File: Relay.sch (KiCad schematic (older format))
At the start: 0 parts

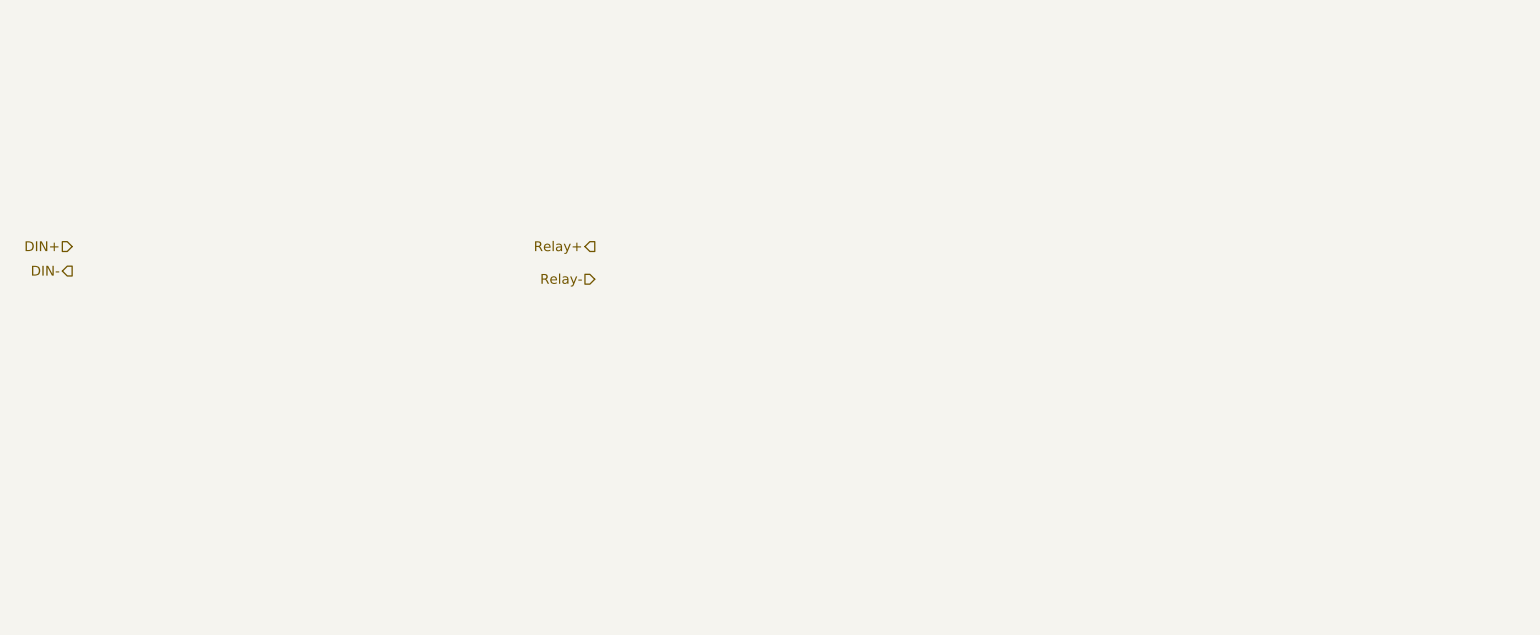
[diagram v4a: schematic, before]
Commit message: Added Relay Driver
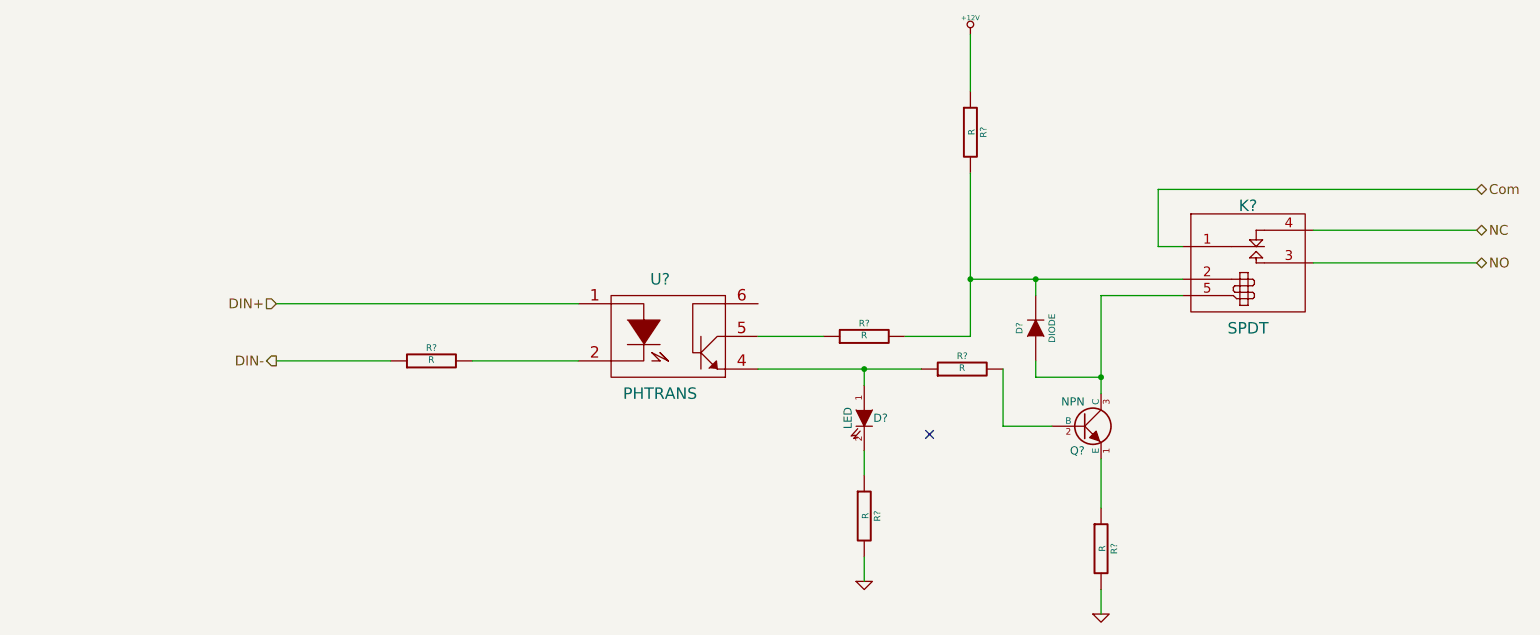
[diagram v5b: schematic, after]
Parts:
- added D?: LED, ~, symbol LED
- added D?: DIODE, ~, symbol DIODE
- added K?: SPDT, ~, symbol SPDT
- added Q?: NPN, ~, symbol NPN
- added R? (x6): R, ~, symbol R
- added U?: PHTRANS, ~, symbol PHTRANS
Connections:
- net DIN+: now also U?.1
- net DIN-: now also R?.1
- new net: R?.2, U?.2
- new net: D?.1 (A), R?.1, U?.4
- new net: R?.1, U?.5
- new net: Q?.1 (E), R?.1
- new net: Q?.2 (B), R?.2
- new net: D?.1 (A), K?.5 (Coil-), Q?.3 (C)
- new net: D?.2 (K), R?.1
- new net: D?.2 (K), K?.2 (Coil-), R?.2, R?.2
- new net +12V: R?.1
- new net Com: K?.1 (Com)
- new net GND: R?.2, R?.2
- new net NC: K?.4 (NC)
- new net NO: K?.3 (NO)
- no-connect marks 0 -> 1
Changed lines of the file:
@@
 LIBS:contrib
 LIBS:valves
+LIBS:arduino_shieldsNCL
+LIBS:spdt
 LIBS:InitialKiCadProject-cache
 EELAYER 27 0
@@
 Comment4 ""
 $EndDescr
-Text HLabel 5350 2800 0    60   Input ~ 0
-Relay-
-Text HLabel 5350 2600 0    60   Output ~ 0
-Relay+
-Text HLabel 2150 2750 0    60   Output ~ 0
+Text HLabel 10750 2700 2    60   BiDi ~ 0
+NO
+Text HLabel 10750 2500 2    60   BiDi ~ 0
+NC
+Text HLabel 3400 3300 0    60   Output ~ 0
 DIN-
-Text HLabel 2150 2600 0    60   Input ~ 0
+Text HLabel 3400 2950 0    60   Input ~ 0
 DIN+
+$Comp
+L PHTRANS U?
+U 1 1 52F444EE
+P 5800 3150
+F 0 "U?" H 5750 3500 70  0000 C CNN
+F 1 "PHTRANS" H 5750 2800 70  0000 C CNN
+F 2 "~" H 5800 3150 60  0000 C CNN
+F 3 "~" H 5800 3150 60  0000 C CNN
+	1    5800 3150
+	1    0    0    -1
+$EndComp
+$Comp
+L NPN Q?
+U 1 1 52F4450C
+P 8350 3700
+F 0 "Q?" H 8350 3550 50  0000 R CNN
+F 1 "NPN" H 8350 3850 50  0000 R CNN
+F 2 "~" H 8350 3700 60  0000 C CNN
+F 3 "~" H 8350 3700 60  0000 C CNN
+	1    8350 3700
+	1    0    0    -1
+$EndComp
+$Comp
+L R R?
+U 1 1 52F4451B
+P 7600 3350
+F 0 "R?" V 7680 3350 40  0000 C CNN
+F 1 "R" V 7607 3351 40  0000 C CNN
+F 2 "~" V 7530 3350 30  0000 C CNN
+F 3 "~" H 7600 3350 30  0000 C CNN
+	1    7600 3350
+	0    -1   -1   0
+$EndComp
+$Comp
+L LED D?
+U 1 1 52F4452A
+P 7000 3650
+F 0 "D?" V 7000 3750 50  0000 C CNN
+F 1 "LED" H 7000 3550 50  0000 C CNN
+F 2 "~" H 7000 3650 60  0000 C CNN
+F 3 "~" H 7000 3650 60  0000 C CNN
+	1    7000 3650
+	0    1    1    0
+$EndComp
+$Comp
+L SPDT K?
+U 1 1 52F44B09
+P 9350 2700
+F 0 "K?" H 9350 3050 70  0000 C CNN
+F 1 "SPDT" H 9350 2300 70  0000 C CNN
+F 2 "~" H 9350 2850 60  0000 C CNN
+F 3 "~" H 9350 2850 60  0000 C CNN
+	1    9350 2700
+	1    0    0    -1
+$EndComp
+Text HLabel 10750 2250 2    60   BiDi ~ 0
+Com
+Wire Wire Line
+	10750 2500 9750 2500
+Wire Wire Line
+	9750 2700 10750 2700
+Wire Wire Line
+	6350 3350 7350 3350
+Wire Wire Line
+	8950 2900 8450 2900
+Wire Wire Line
+	8450 2900 8450 3500
+$Comp
+L R R?
+U 1 1 52F44CA5
+P 8450 4450
+F 0 "R?" V 8530 4450 40  0000 C CNN
+F 1 "R" V 8457 4451 40  0000 C CNN
+F 2 "~" V 8380 4450 30  0000 C CNN
+F 3 "~" H 8450 4450 30  0000 C CNN
+	1    8450 4450
+	1    0    0    -1
+$EndComp
+Wire Wire Line
+	8450 3900 8450 4200
+$Comp
+L GND #PWR?
+U 1 1 52F44CBC
+P 8450 4850
+F 0 "#PWR?" H 8450 4850 30  0001 C CNN
+F 1 "GND" H 8450 4780 30  0001 C CNN
+F 2 "" H 8450 4850 60  0000 C CNN
+F 3 "" H 8450 4850 60  0000 C CNN
+	1    8450 4850
+	1    0    0    -1
+$EndComp
+Wire Wire Line
+	8450 4700 8450 4850
+$Comp
+L R R?
+U 1 1 52F44D04
+P 7000 4250
+F 0 "R?" V 7080 4250 40  0000 C CNN
+F 1 "R" V 7007 4251 40  0000 C CNN
+F 2 "~" V 6930 4250 30  0000 C CNN
+F 3 "~" H 7000 4250 30  0000 C CNN
+	1    7000 4250
+	1    0    0    -1
+$EndComp
+$Comp
+L GND #PWR?
+U 1 1 52F44D0A
+P 7000 4650
+F 0 "#PWR?" H 7000 4650 30  0001 C CNN
+F 1 "GND" H 7000 4580 30  0001 C CNN
+F 2 "" H 7000 4650 60  0000 C CNN
+F 3 "" H 7000 4650 60  0000 C CNN
+	1    7000 4650
+	1    0    0    -1
+$EndComp
+Wire Wire Line
+	7000 4500 7000 4650
+Wire Wire Line
+	7000 3850 7000 4000
+Wire Wire Line
+	7000 3450 7000 3350
+Connection ~ 7000 3350
+NoConn ~ 7400 3750
+$Comp
+L R R?
+U 1 1 52F44D31
+P 7650 1900
+F 0 "R?" V 7730 1900 40  0000 C CNN
+F 1 "R" V 7657 1901 40  0000 C CNN
+F 2 "~" V 7580 1900 30  0000 C CNN
+F 3 "~" H 7650 1900 30  0000 C CNN
+	1    7650 1900
+	1    0    0    -1
+$EndComp
+Wire Wire Line
+	7650 2150 7650 3150
+Wire Wire Line
+	7650 2800 8950 2800
+$Comp
+L R R?
+U 1 1 52F44D45
+P 7000 3150
+F 0 "R?" V 7080 3150 40  0000 C CNN
+F 1 "R" V 7007 3151 40  0000 C CNN
+F 2 "~" V 6930 3150 30  0000 C CNN
+F 3 "~" H 7000 3150 30  0000 C CNN
+	1    7000 3150
+	0    -1   -1   0
+$EndComp
+Wire Wire Line
+	6350 3150 6750 3150
+Wire Wire Line
+	7650 3150 7250 3150
+Connection ~ 7650 2800
+$Comp
+L +12V #PWR?
+U 1 1 52F44D6F
+P 7650 1300
+F 0 "#PWR?" H 7650 1250 20  0001 C CNN
+F 1 "+12V" H 7650 1400 30  0000 C CNN
+F 2 "" H 7650 1300 60  0000 C CNN
+F 3 "" H 7650 1300 60  0000 C CNN
+	1    7650 1300
+	1    0    0    -1
+$EndComp
+Wire Wire Line
+	7650 1300 7650 1650
+$Comp
+L R R?
+U 1 1 52F44D8F
+P 4350 3300
+F 0 "R?" V 4430 3300 40  0000 C CNN
+F 1 "R" V 4357 3301 40  0000 C CNN
+F 2 "~" V 4280 3300 30  0000 C CNN
+F 3 "~" H 4350 3300 30  0000 C CNN
+	1    4350 3300
+	0    -1   -1   0
+$EndComp
+Wire Wire Line
+	4600 3300 5250 3300
+Wire Wire Line
+	3400 3300 4100 3300
+Wire Wire Line
+	3400 2950 5250 2950
+Wire Wire Line
+	10750 2250 8800 2250
+Wire Wire Line
+	8800 2250 8800 2600
+Wire Wire Line
+	8800 2600 8950 2600
+$Comp
+L DIODE D?
+U 1 1 52F44E37
+P 8050 3100
+F 0 "D?" H 8050 3200 40  0000 C CNN
+F 1 "DIODE" H 8050 3000 40  0000 C CNN
+F 2 "~" H 8050 3100 60  0000 C CNN
+F 3 "~" H 8050 3100 60  0000 C CNN
+	1    8050 3100
+	0    -1   -1   0
+$EndComp
+Wire Wire Line
+	7850 3350 7850 3700
+Wire Wire Line
+	7850 3700 8150 3700
+Wire Wire Line
+	8050 2900 8050 2800
+Connection ~ 8050 2800
+Wire Wire Line
+	8050 3300 8050 3400
+Wire Wire Line
+	8050 3400 8450 3400
+Connection ~ 8450 3400
 $EndSCHEMATC

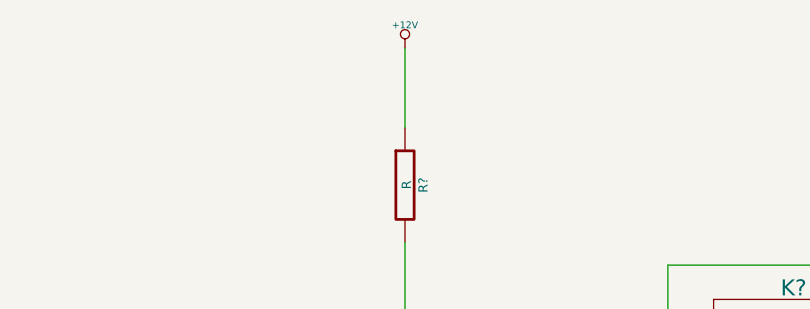
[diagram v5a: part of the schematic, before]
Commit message: added filter power section
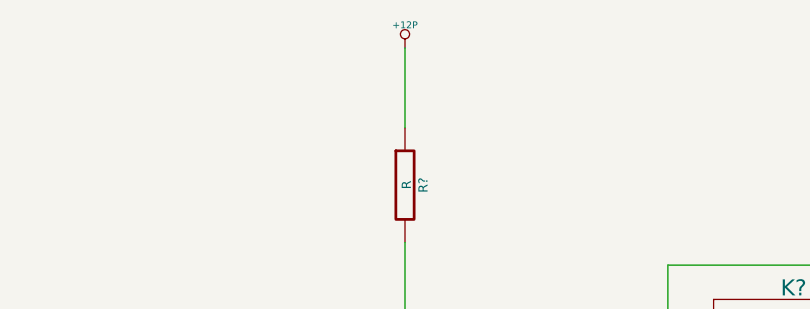
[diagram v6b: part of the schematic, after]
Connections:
- net +12V renamed +12P
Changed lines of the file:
@@
 LIBS:arduino_shieldsNCL
 LIBS:spdt
+LIBS:BenchLib
 LIBS:InitialKiCadProject-cache
 EELAYER 27 0
@@
 $Descr A4 11693 8268
 encoding utf-8
-Sheet 6 8
+Sheet 6 9
 Title ""
 Date "7 feb 2014"
@@
 	7650 3150 7250 3150
 Connection ~ 7650 2800
-$Comp
-L +12V #PWR?
-U 1 1 52F44D6F
-P 7650 1300
-F 0 "#PWR?" H 7650 1250 20  0001 C CNN
-F 1 "+12V" H 7650 1400 30  0000 C CNN
-F 2 "" H 7650 1300 60  0000 C CNN
-F 3 "" H 7650 1300 60  0000 C CNN
-	1    7650 1300
-	1    0    0    -1
-$EndComp
 Wire Wire Line
 	7650 1300 7650 1650
@@
 	8050 3400 8450 3400
 Connection ~ 8450 3400
+$Comp
+L +12P #PWR?
+U 1 1 52F4581E
+P 7650 1300
+F 0 "#PWR?" H 7650 1270 30  0001 C CNN
+F 1 "+12P" H 7650 1400 30  0000 C CNN
+F 2 "" H 7650 1300 60  0000 C CNN
+F 3 "" H 7650 1300 60  0000 C CNN
+	1    7650 1300
+	1    0    0    -1
+$EndComp
 $EndSCHEMATC

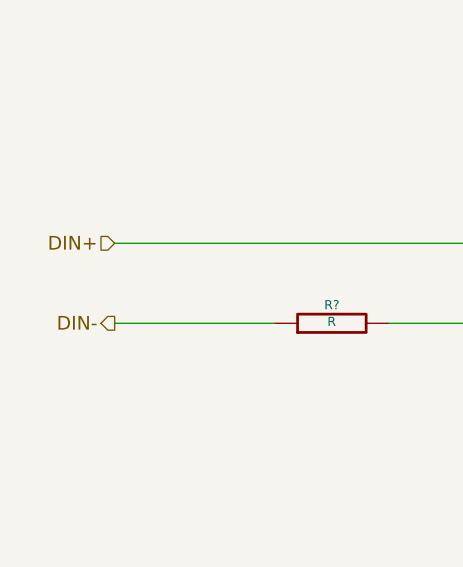
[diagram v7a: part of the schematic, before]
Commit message: WIRED BLOCK DIAGRAM TOGETHER AND ADDED ARDUINO BLOCK
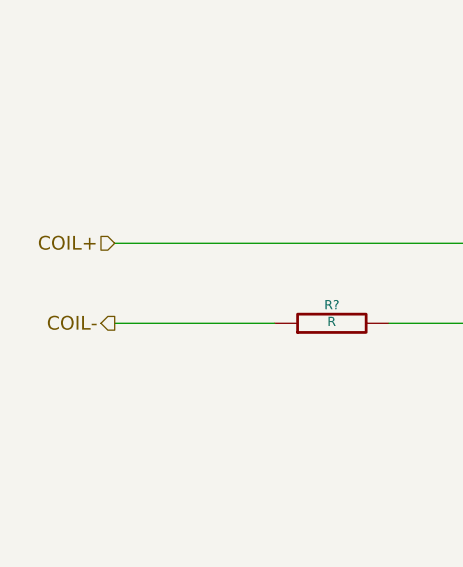
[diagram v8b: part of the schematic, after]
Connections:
- net DIN+ renamed COIL+
- net DIN- renamed COIL-
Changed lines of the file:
@@
-EESchema Schematic File Version 2  date Sat 08 Feb 2014 08:25:16 PM EST
+EESchema Schematic File Version 2  date Sat 08 Feb 2014 11:37:49 PM EST
 LIBS:power
 LIBS:device
@@
 Comment4 ""
 $EndDescr
+Wire Wire Line
+	10750 2500 9750 2500
+Wire Wire Line
+	9750 2700 10750 2700
+Wire Wire Line
+	6350 3350 7350 3350
+Wire Wire Line
+	8950 2900 8450 2900
+Wire Wire Line
+	8450 2900 8450 3500
+Wire Wire Line
+	8450 3900 8450 4200
+Wire Wire Line
+	8450 4700 8450 4850
+Wire Wire Line
+	7000 4500 7000 4650
+Wire Wire Line
+	7000 3850 7000 4000
+Wire Wire Line
+	7000 3450 7000 3350
+Connection ~ 7000 3350
+Wire Wire Line
+	7650 2150 7650 3150
+Wire Wire Line
+	7650 2800 8950 2800
+Wire Wire Line
+	6350 3150 6750 3150
+Wire Wire Line
+	7650 3150 7250 3150
+Connection ~ 7650 2800
+Wire Wire Line
+	7650 1300 7650 1650
+Wire Wire Line
+	4600 3300 5250 3300
+Wire Wire Line
+	3400 3300 4100 3300
+Wire Wire Line
+	3400 2950 5250 2950
+Wire Wire Line
+	10750 2250 8800 2250
+Wire Wire Line
+	8800 2250 8800 2600
+Wire Wire Line
+	8800 2600 8950 2600
+Wire Wire Line
+	7850 3350 7850 3700
+Wire Wire Line
+	7850 3700 8150 3700
+Wire Wire Line
+	8050 2900 8050 2800
+Connection ~ 8050 2800
+Wire Wire Line
+	8050 3300 8050 3400
+Wire Wire Line
+	8050 3400 8450 3400
+Connection ~ 8450 3400
 Text HLabel 10750 2700 2    60   BiDi ~ 0
 NO
@@
 NC
 Text HLabel 3400 3300 0    60   Output ~ 0
-DIN-
+COIL-
 Text HLabel 3400 2950 0    60   Input ~ 0
-DIN+
+COIL+
 $Comp
 L PHTRANS U?
@@
 Text HLabel 10750 2250 2    60   BiDi ~ 0
 Com
-Wire Wire Line
-	10750 2500 9750 2500
-Wire Wire Line
-	9750 2700 10750 2700
-Wire Wire Line
-	6350 3350 7350 3350
-Wire Wire Line
-	8950 2900 8450 2900
-Wire Wire Line
-	8450 2900 8450 3500
 $Comp
 L R R?
@@
 	1    0    0    -1
 $EndComp
-Wire Wire Line
-	8450 3900 8450 4200
 $Comp
 L GND #PWR?
@@
 	1    0    0    -1
 $EndComp
-Wire Wire Line
-	8450 4700 8450 4850
 $Comp
 L R R?
@@
 	1    0    0    -1
 $EndComp
-Wire Wire Line
-	7000 4500 7000 4650
-Wire Wire Line
-	7000 3850 7000 4000
-Wire Wire Line
-	7000 3450 7000 3350
-Connection ~ 7000 3350
 NoConn ~ 7400 3750
 $Comp
@@
 	1    0    0    -1
 $EndComp
-Wire Wire Line
-	7650 2150 7650 3150
-Wire Wire Line
-	7650 2800 8950 2800
 $Comp
 L R R?
@@
 	0    -1   -1   0
 $EndComp
-Wire Wire Line
-	6350 3150 6750 3150
-Wire Wire Line
-	7650 3150 7250 3150
-Connection ~ 7650 2800
-Wire Wire Line
-	7650 1300 7650 1650
 $Comp
 L R R?
@@
 	0    -1   -1   0
 $EndComp
-Wire Wire Line
-	4600 3300 5250 3300
-Wire Wire Line
-	3400 3300 4100 3300
-Wire Wire Line
-	3400 2950 5250 2950
-Wire Wire Line
-	10750 2250 8800 2250
-Wire Wire Line
-	8800 2250 8800 2600
-Wire Wire Line
-	8800 2600 8950 2600
 $Comp
 L DIODE D?
@@
 	0    -1   -1   0
 $EndComp
-Wire Wire Line
-	7850 3350 7850 3700
-Wire Wire Line
-	7850 3700 8150 3700
-Wire Wire Line
-	8050 2900 8050 2800
-Connection ~ 8050 2800
-Wire Wire Line
-	8050 3300 8050 3400
-Wire Wire Line
-	8050 3400 8450 3400
-Connection ~ 8450 3400
 $Comp
 L +12P #PWR?
